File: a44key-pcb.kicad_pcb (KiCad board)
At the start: 2 copper layers, 118.7 x 105.5 mm, 74 parts, among them J1 AudioJack3, J2 Conn_01x04_Female, J3 Conn_01x04_Female, SW1 SW_Push, U1 ATmega32U4-AU, Y1 16MHz

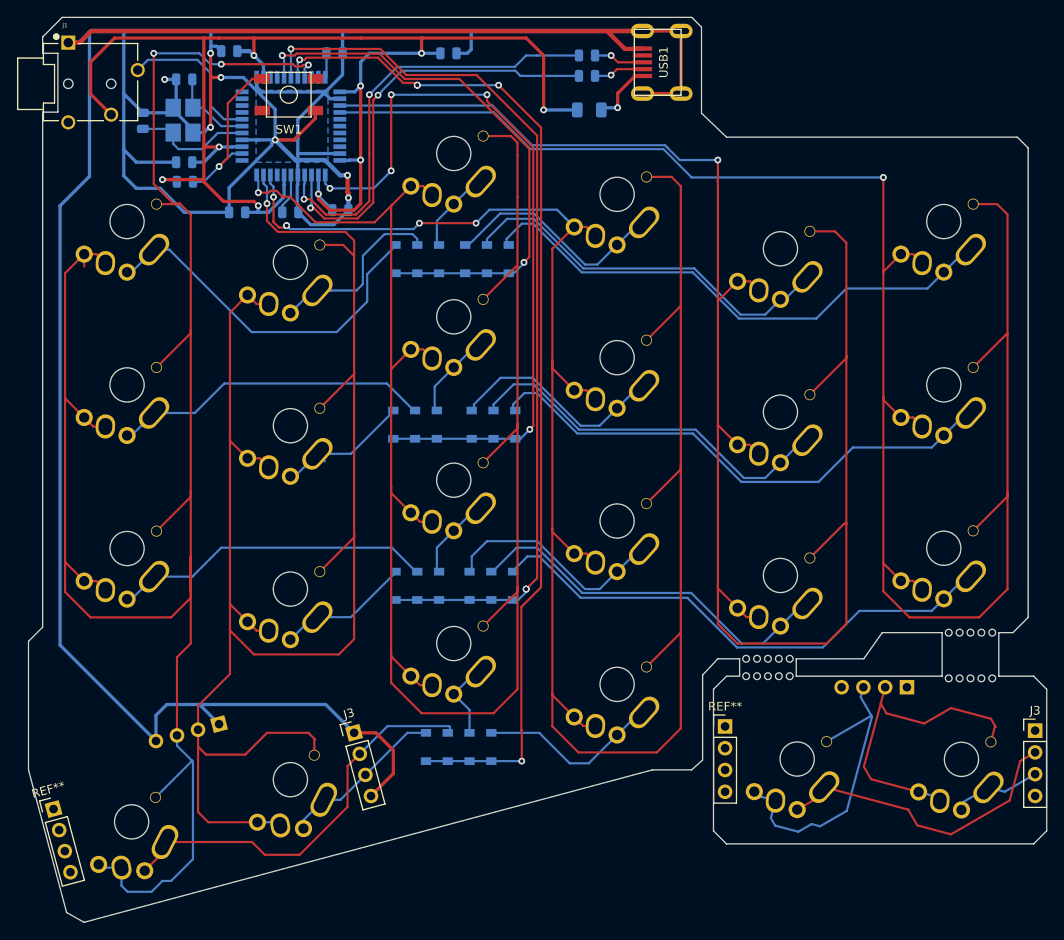
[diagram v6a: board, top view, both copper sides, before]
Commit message: Added the footprint libraries
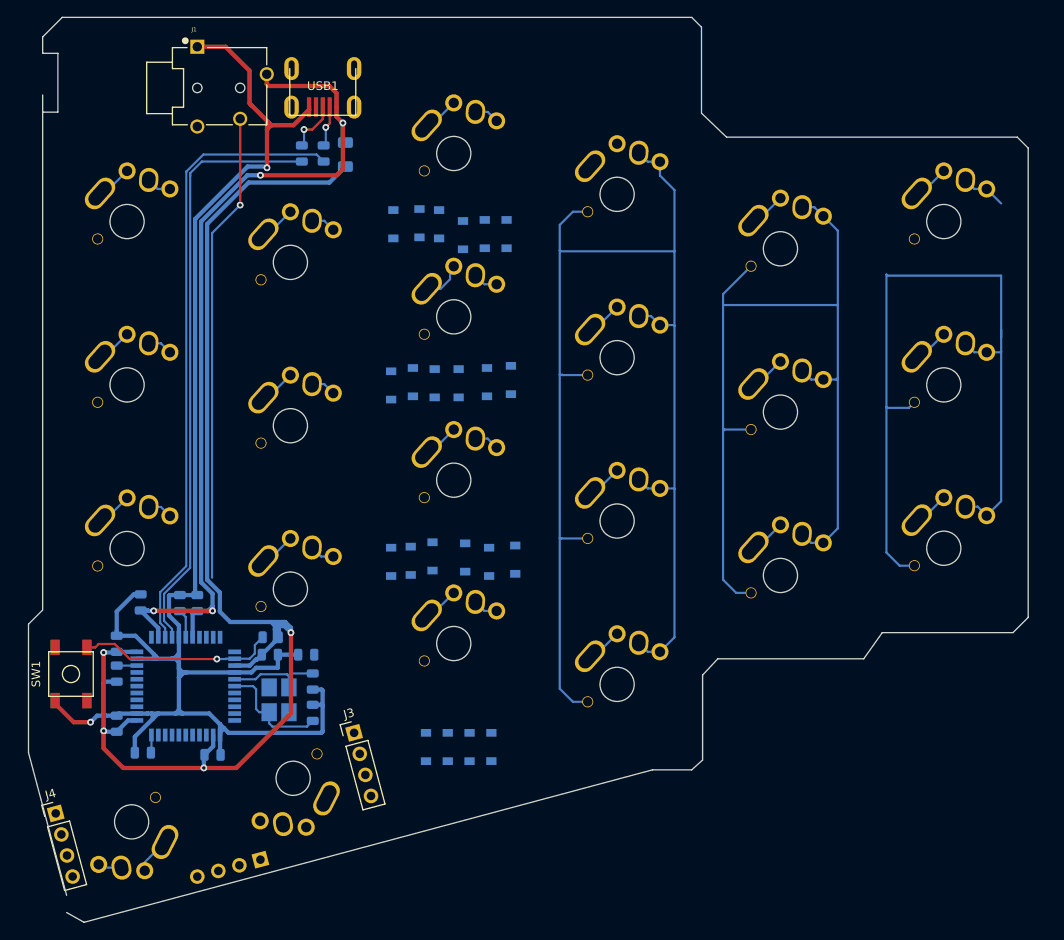
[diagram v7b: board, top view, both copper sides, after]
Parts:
- removed the J2 at (185.9, 124.5)
- removed the J3 at (200.8, 129.5)
- removed the MX4 at (173.1, 132.8)
- removed the MX8 at (192.2, 132.9)
- removed the MX8 at (114.0, 135.3)
- removed REF** (x4): breakaway-mousebites, random-keyboard-parts:breakaway-mousebites
- removed REF** (x2): PinHeader_1x04_P2.54mm_Vertical, Connector_PinHeader_2.54mm:PinHeader_1x04_P2.54mm_Vertical
- added C11: 0.1uF, Capacitor_SMD:C_0805_2012Metric, B.Cu at (93.7, 122.9)
- added C9: 1uF, Capacitor_SMD:C_0805_2012Metric, B.Cu at (103.1, 114.7)
- added J4: Conn_01x04_Female, Connector_PinHeader_2.54mm:PinHeader_1x04_P2.54mm_Vertical, F.Cu at (86.6, 139.2)
- added MX8: MX-NoLED, MX_Alps_Hybrid:MX-Alps-Choc-X-1U-NoLED, F.Cu at (114.3, 135.1)
- added R5: 10k, Resistor_SMD:R_0805_2012Metric, B.Cu at (115.8, 120.7)
- moved R4 84.6 mm to (96.8, 132.1), turned to 0 degrees
- moved C2 75.4 mm to (116.6, 127.5), turned to 90 degrees
- moved C7 73.4 mm to (96.5, 114.6), turned to 90 degrees
- moved SW1 72.2 mm to (88.4, 122.9), turned to 270 degrees
- moved C4 70.5 mm to (111.6, 120.7), turned to 0 degrees
- moved Y1 68.5 mm to (112.7, 125.9), turned to 90 degrees
- moved C3 68.3 mm to (116.6, 123.8), turned to 270 degrees
- moved U1 66.5 mm to (101.8, 124.3), turned to 270 degrees
- moved C8 65.3 mm to (104.9, 132.4)
- moved C1 61.3 mm to (93.7, 128.7), turned to 90 degrees
- moved C5 56.7 mm to (93.7, 119.4), turned to 90 degrees
- moved R3 54.1 mm to (111.7, 118.7), turned to 180 degrees
- moved C6 47.4 mm to (101.1, 114.7), turned to 90 degrees
- moved USB1 41.8 mm to (117.8, 52.3), turned to 270 degrees
- moved R2 35.2 mm to (115.3, 62.2), turned to 90 degrees
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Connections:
- C1 pad 1: +5V -> VCC
- C4 pad 1: +5V -> VCC
- C5 pad 1: +5V -> VCC
- C8 pad 1: +5V -> VCC
- F1 pad 1: +5V -> VCC
- F1 pad 2: VCC -> +5V
- J1 pad 2: +5V -> SCL
- J1 pad 3: SCL -> +5V
- J2 pad 1: GND -> Net-(J2-Pad1)
- J2 pad 4: GND -> Net-(J2-Pad4)
- J3 pad 1: GND -> Net-(J3-Pad1)
- J3 pad 4: GND -> Net-(J3-Pad4)
- R3 pad 1: +5V -> VCC
- U1 pad 14: +5V -> VCC
- U1 pad 24: +5V -> VCC
- U1 pad 34: +5V -> VCC
- U1 pad 44: +5V -> VCC
- USB1 pad 5: VCC -> +5V
- USB1 pad 6: GND -> Net-(USB1-Pad6)
- Y1 pad 2: GND -> Net-(Y1-Pad2)
- Y1 pad 4: GND -> Net-(Y1-Pad4)
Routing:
- net GND: track 460.6 -> 194.6 mm, vias 7 -> 2
- net COL5: track 237.4 -> 11.5 mm, vias 3 -> 0
- net COL4: track 202.4 -> 8.73 mm, vias 1 -> 0
- net COL3: track 205.2 -> 12.5 mm, vias 1 -> 0
- net VCC: track 7.42 -> 147.7 mm, vias 1 -> 4
- net ROW3: track 119.3 -> 0.00 mm, vias 5 -> 0
- net (no net): track 119.2 -> 0.00 mm
- net COL0: track 209.4 -> 95.7 mm, vias 1 -> 0
- net ROW2: track 105.6 -> 0.00 mm, vias 3 -> 0
- net COL1: track 198.3 -> 108.5 mm, vias 1 -> 0
- net ROW1: track 87.6 -> 0.00 mm, vias 5 -> 0
- net COL2: track 228.9 -> 155.5 mm, vias 5 -> 0
- net +5V: track 171.5 -> 104.4 mm, vias 9 -> 4
- net ROW0: track 64.9 -> 0.00 mm, vias 2 -> 0
- net Net-(D20-Pad2): track 63.5 -> 4.24 mm
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- removed copper zone on B.Cu, net GND
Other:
- board size 118.7 x 105.5 mm -> 116.6 x 105.5 mm
- net class Power: trace_width 0.381 -> 0.5

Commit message: {PCB
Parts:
- moved R2 0.25 mm to (115.6, 62.2)
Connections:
- MX4 pad 1: COL5 -> TH35
- MX4 pad 2: TH35 -> COL5
- MX8 pad 1: COL4 -> TH34
- MX8 pad 2: TH34 -> COL4
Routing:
- net COL3: track 12.5 -> 189.7 mm
- net COL5: track 11.5 -> 167.2 mm
- net COL4: track 8.73 -> 158.9 mm
- net COL0: track 95.7 -> 133.4 mm
- net COL2: track 155.5 -> 185.7 mm
- net COL1: track 108.5 -> 137.1 mm
- net SCL: track 54.9 -> 77.5 mm, vias 1 -> 3
- net Net-(USB1-Pad6): track 0.00 -> 16.3 mm
- net TH35: track 4.33 -> 2.82 mm
- net Net-(R1-Pad1): track 73.0 -> 71.7 mm, vias 0 -> 2
- net Net-(D13-Pad2): track 0.00 -> 1.23 mm
- net VCC: track 147.7 -> 147.4 mm, vias 4 -> 6
- net Net-(R2-Pad1): track 69.5 -> 69.6 mm, vias 0 -> 2
- net +5V: track 104.4 -> 104.3 mm, vias 4 -> 3
